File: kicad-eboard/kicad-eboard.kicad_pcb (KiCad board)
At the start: 2 copper layers, 93 parts, among them J1 Conn_02x03, J2 Conn_01x02, J3 Conn_01x10, M1 Hopper_Servo, SW1 LIMIT_1, SW2 LIMIT_2, SW3 SRX_Encoder, U1 TinkerBoard, U10 REF2033, U11 PDQ15-Q24-S12-D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

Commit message: More routing, moving components
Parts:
- C20, C21, R12, R15: moved to B.Cu
- moved TP5 90.6 mm to (72.6, 93.8)
- moved TP6 90.6 mm to (69.6, 93.8)
- moved H1 71.5 mm to (28.4, 36.9)
- moved H2 71.5 mm to (28.4, 94.9)
- moved H3 71.5 mm to (77.4, 36.9)
- moved H4 71.5 mm to (77.4, 94.9)
- moved R15 68.0 mm to (56.1, 81.2), turned to 180 degrees
- moved R12 66.4 mm to (59.8, 81.2), turned to 0 degrees
- moved TP13 55.3 mm to (69.5, 35.2)
- moved TP1 52.1 mm to (28.9, 23.9)
- moved TP12 42.2 mm to (92.4, 38.2), turned to 270 degrees
- moved TP14 37.8 mm to (71.9, 30.9)
- moved TP15 37.8 mm to (71.9, 27.6)
- moved TP9 34.3 mm to (65.1, 18.3), turned to 0 degrees
- moved TP11 33.6 mm to (92.4, 31.5), turned to 90 degrees
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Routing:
- net /M1+: track 15.0 -> 13.8 mm

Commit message: Finish routing?
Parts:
- moved C3 52.8 mm to (29.8, 103.7)
- moved M1 28.8 mm to (46.5, 102.2)
- moved TP15 21.6 mm to (79.7, 47.7), turned to 270 degrees
- moved RV1 17.7 mm to (57.6, 102.2)
- moved RV2 17.7 mm to (68.6, 102.2)
- moved RV3 17.7 mm to (79.6, 102.2)
- moved L1 15.3 mm to (47.5, 54.8)
- moved TP12 13.3 mm to (79.6, 41.8)
- moved C9 12.9 mm to (58.8, 19.6)
- moved TP11 12.5 mm to (80.0, 32.5)
- moved C12 11.7 mm to (48.9, 21.5)
- moved C16 11.0 mm to (42.8, 23.4)
- moved TP13 8.64 mm to (76.2, 29.8), turned to 270 degrees
- moved C14 6.86 mm to (44.9, 23.4), turned to 270 degrees
- moved SW3 5.41 mm to (30.6, 41.6), turned to 270 degrees
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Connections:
- U1 pad 16: Net-(U1-Pad16) -> /IMU/INT
- U1 pad 27: /IMU/INT -> Net-(U1-Pad27)
- U8 pad 4: Net-(RV1-Pad2) -> Net-(M1-Pad4)
- U8 pad 5: Net-(RV2-Pad2) -> Net-(RV1-Pad2)
- U8 pad 6: Net-(RV3-Pad2) -> Net-(RV2-Pad2)
- U8 pad 7: Net-(M1-Pad4) -> Net-(RV3-Pad2)
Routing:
- net +5V: track 9.19 -> 202.8 mm, vias 1 -> 2
- net GNDA: track 0.00 -> 163.3 mm
- net +12V: track 0.00 -> 140.7 mm
- net +3V3: track 67.0 -> 188.9 mm, vias 3 -> 4
- net GND: track 47.1 -> 133.5 mm, vias 2 -> 4
- net GNDPWR: track 0.00 -> 84.2 mm
- net /SDA: track 28.3 -> 97.5 mm
- net /SCL: track 38.8 -> 101.6 mm, vias 0 -> 1
- net Net-(TP1-Pad1): track 0.00 -> 60.6 mm, vias 0 -> 1
- net +BATT: track 0.00 -> 54.1 mm
- net Net-(C20-Pad1): track 0.00 -> 52.4 mm
- net /SCLK: track 11.7 -> 60.0 mm, vias 0 -> 1
- net /MISO: track 6.95 -> 52.9 mm, vias 0 -> 1
- net /SS: track 6.24 -> 51.2 mm, vias 0 -> 1
- net /MOSI: track 3.28 -> 46.9 mm, vias 0 -> 1
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- added copper zone on B.Cu, net GND
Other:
- board outline added: 67.2 x 90 mm
- copper layers 2 -> 4

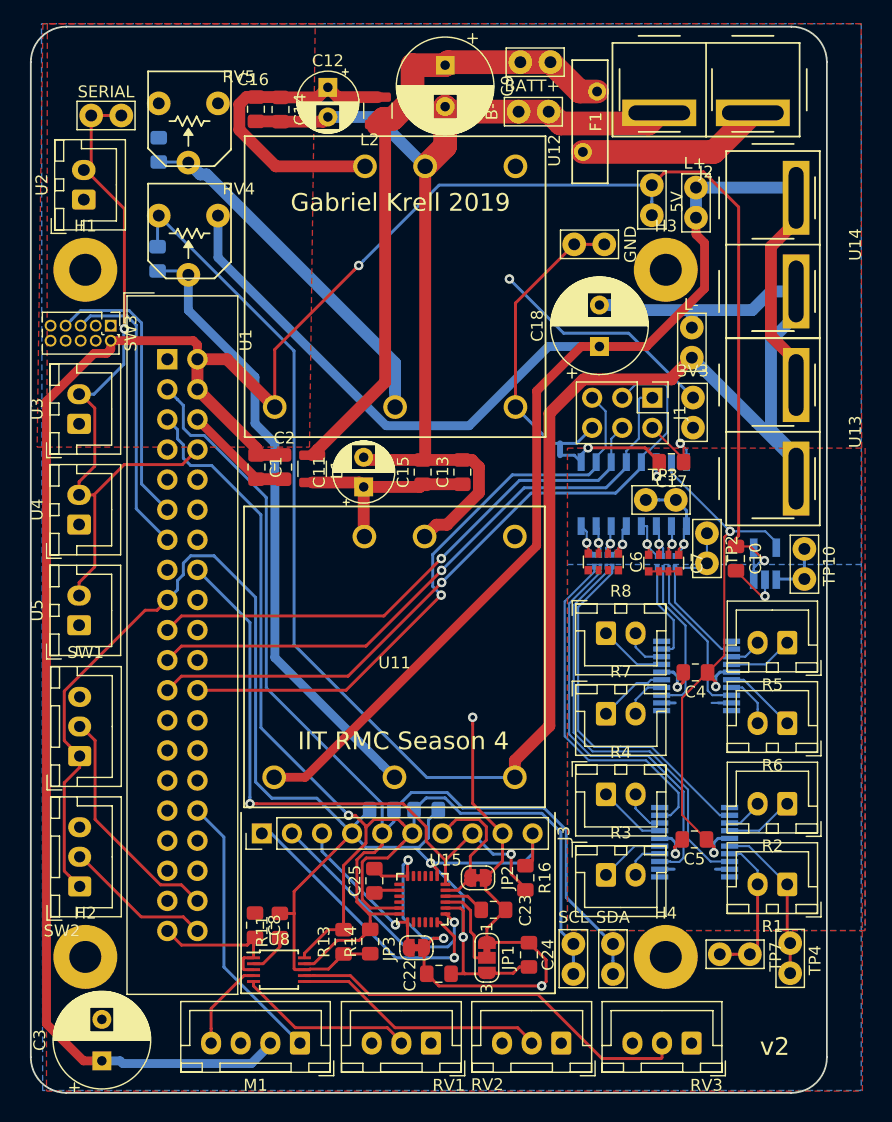
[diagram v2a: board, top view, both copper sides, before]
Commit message: Silkscreen cleanup
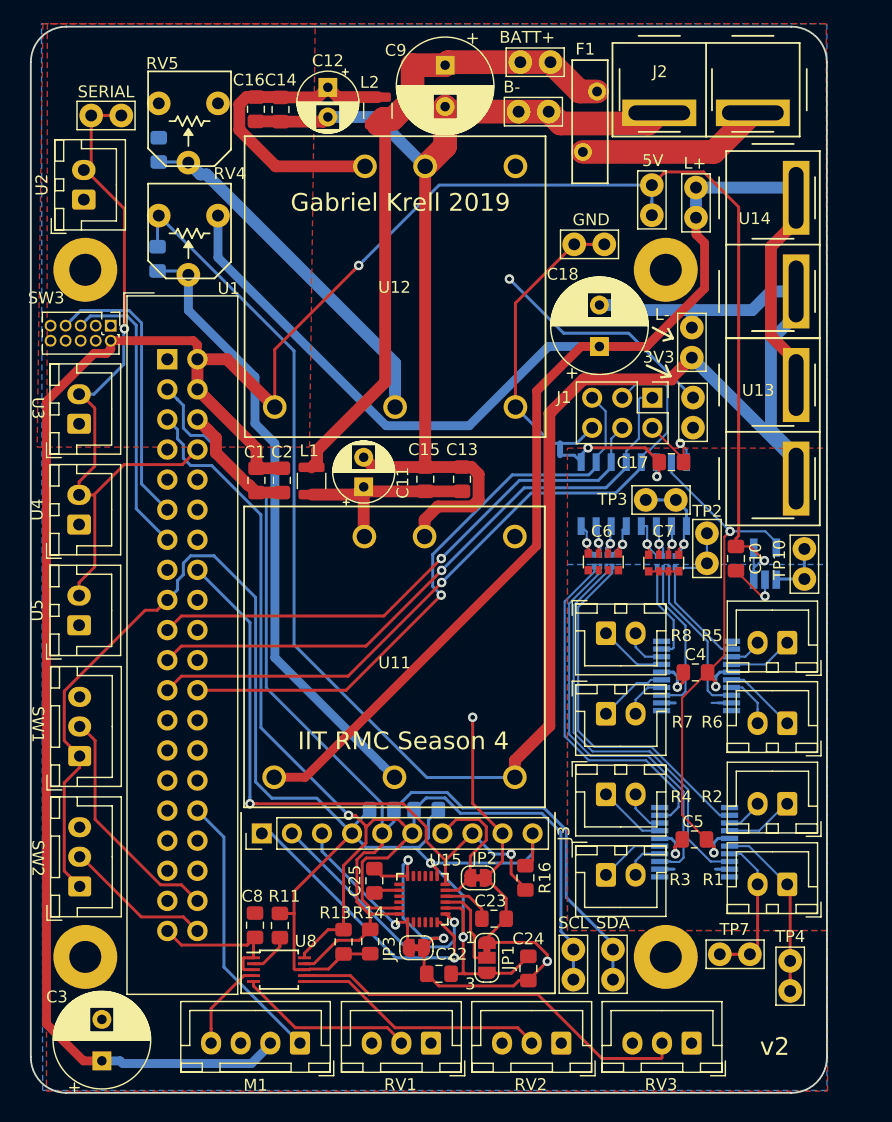
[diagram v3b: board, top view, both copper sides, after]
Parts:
- moved TP4 1.50 mm to (87.9, 97.8)
- moved C24 1.15 mm to (65.8, 95.9), turned to 270 degrees
- moved C2 1.13 mm to (45.0, 54.7)
- moved C1 1.12 mm to (42.9, 54.7)
- moved L1 1.03 mm to (47.5, 55.8)
- moved C23 0.75 mm to (62.9, 91.7)
- moved C15 0.64 mm to (57.1, 54.6)
- moved C13 0.60 mm to (60.2, 54.6)
- moved TP6 0.47 mm to (69.6, 94.3)
- moved TP5 0.47 mm to (72.9, 94.3)
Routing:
- net GNDPWR: track 84.2 -> 85.8 mm
- net /M1+: track 13.8 -> 15.3 mm
- net +BATT: track 54.1 -> 55.2 mm
- net +5V: track 202.8 -> 203.9 mm
- net Net-(C23-Pad1): track 3.50 -> 4.33 mm
- net GND: track 133.5 -> 134.1 mm

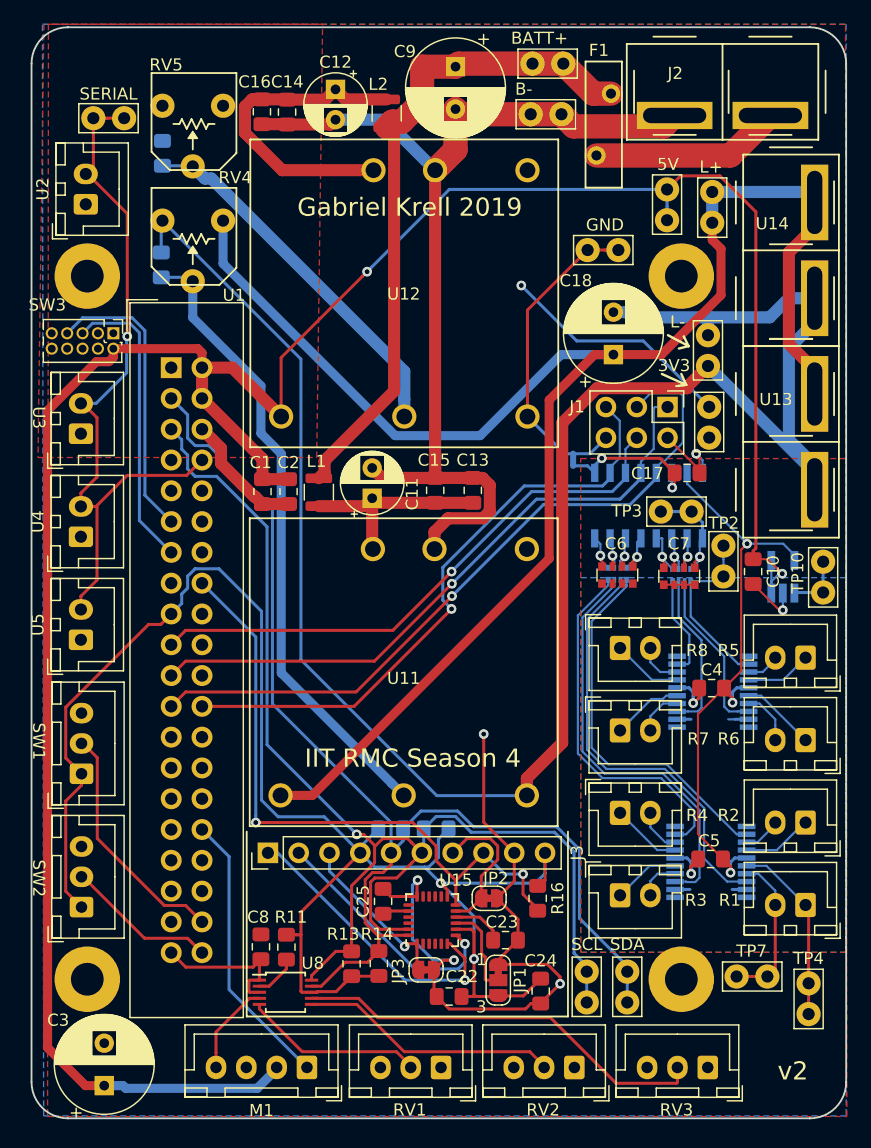
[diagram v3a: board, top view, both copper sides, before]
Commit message: Fix Powerpole 3D/connection issue; more silkscreen
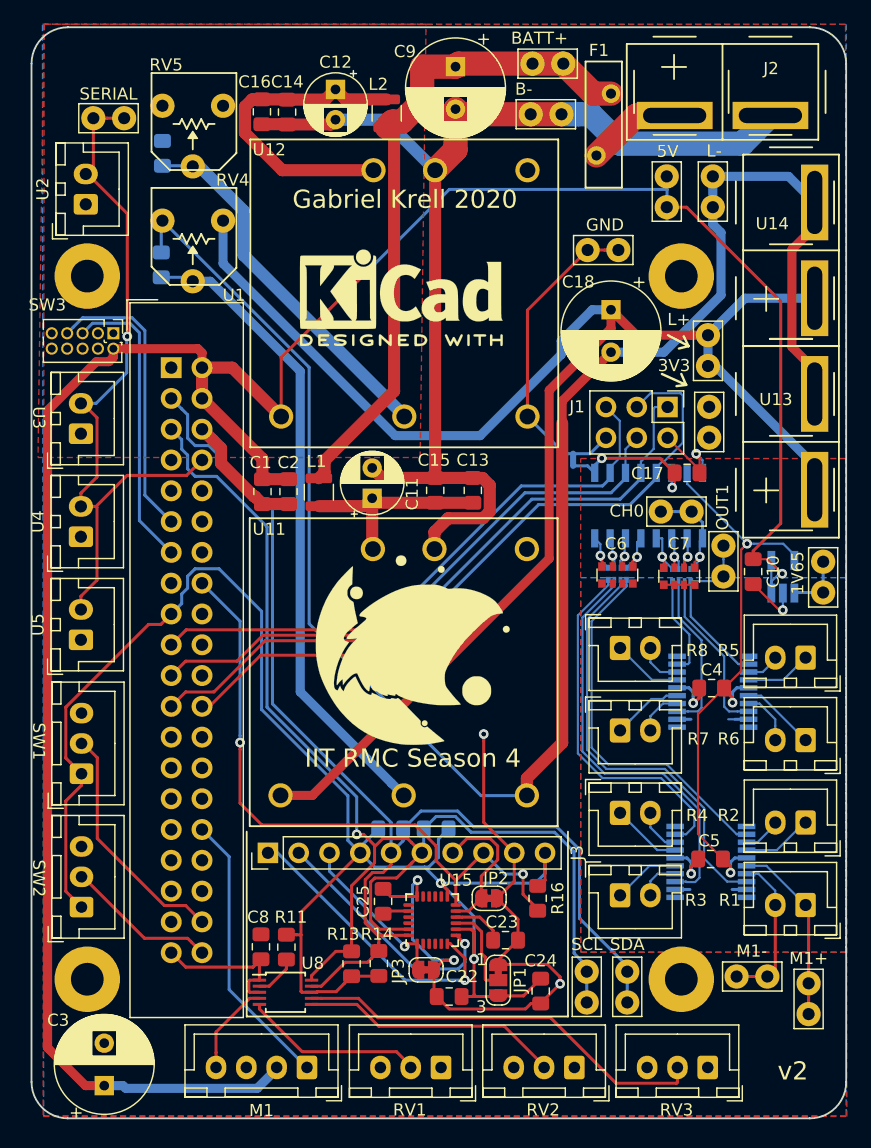
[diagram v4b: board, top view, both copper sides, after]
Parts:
- added G***: LOGO, 2019Spacehawks:SSH_logo, B.Cu at (54.4, 67.1)
- added G***: LOGO, 2019Spacehawks:SSH_logo, F.Cu at (55.4, 67.3)
- added G1: KiCad-Logo2_8mm_SilkScreen, Symbol:KiCad-Logo2_8mm_SilkScreen, B.Cu at (54.9, 38.7)
- added G1: KiCad-Logo2_8mm_SilkScreen, Symbol:KiCad-Logo2_8mm_SilkScreen, F.Cu at (54.3, 38.7)
- moved TP12 13.1 mm to (80.0, 28.7)
- moved TP11 11.8 mm to (79.6, 44.3)
- moved C18 3.71 mm to (71.6, 39.7), turned to 270 degrees
- moved TP13 1.08 mm to (76.2, 28.7)
- renumbered TP10 to 1V65, TP3 to CH0, TP4 to M1+, TP7 to M1-, TP2 to OUT1
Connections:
- J2 pad 1: Net-(F1-Pad1) -> GNDPWR
- J2 pad 2: GNDPWR -> Net-(F1-Pad1)
- U13 pad 1: +12V -> GNDA
- U13 pad 2: GNDA -> +12V
- U14 pad 1: +12V -> GNDA
- U14 pad 2: GNDA -> +12V
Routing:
- net +3V3: track 189.2 -> 167.4 mm, vias 4 -> 3
- net GNDA: track 163.3 -> 151.9 mm
- net GNDPWR: track 85.8 -> 94.9 mm
- net Net-(F1-Pad1): track 15.7 -> 7.82 mm
- net +12V: track 140.7 -> 137.0 mm
- net +5V: track 203.9 -> 200.9 mm
- net /SS: track 51.2 -> 50.2 mm
- net Net-(C20-Pad1): track 52.4 -> 53.2 mm
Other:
- board text added: "Gabriel Krell 2020"
- board text added: "extra I2C pull-ups"
- board text removed: "Gabriel Krell 2019"

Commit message: Fix test point labels (oops)
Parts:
- renumbered 1V65 to TP10, OUT1 to TP2, CH0 to TP3, M1+ to TP4, M1- to TP7

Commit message: Add logo symbols, standardize component values
Added a hacky almost-invisible schematic symbol for graphics, because
otherwise hitting "Update PCB from Schematic" will delete footprints
that aren't in the schematic. Also standardized component values - prefer
100n to 0.1u; prefer 100n to 100nF; prefer 100k to 100K.
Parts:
- C10, C17, C23, C24, C4, C5, C8: value 0.1uF -> 100n
- C22: value 10nF -> 10n
- C25: value 2.2nF -> 2.2n
- C9: value 1000uF -> 1000u
- G1: value KiCad-Logo2_8mm_SilkScreen -> Logo
- G2: renamed from G1; value KiCad-Logo2_8mm_SilkScreen -> Logo
- G3, G4: renamed from G***; value LOGO -> Logo
- R11, R12, R13, R14, R15, R16, RV1, RV2, RV3, RV4, RV5: value 10K -> 10k

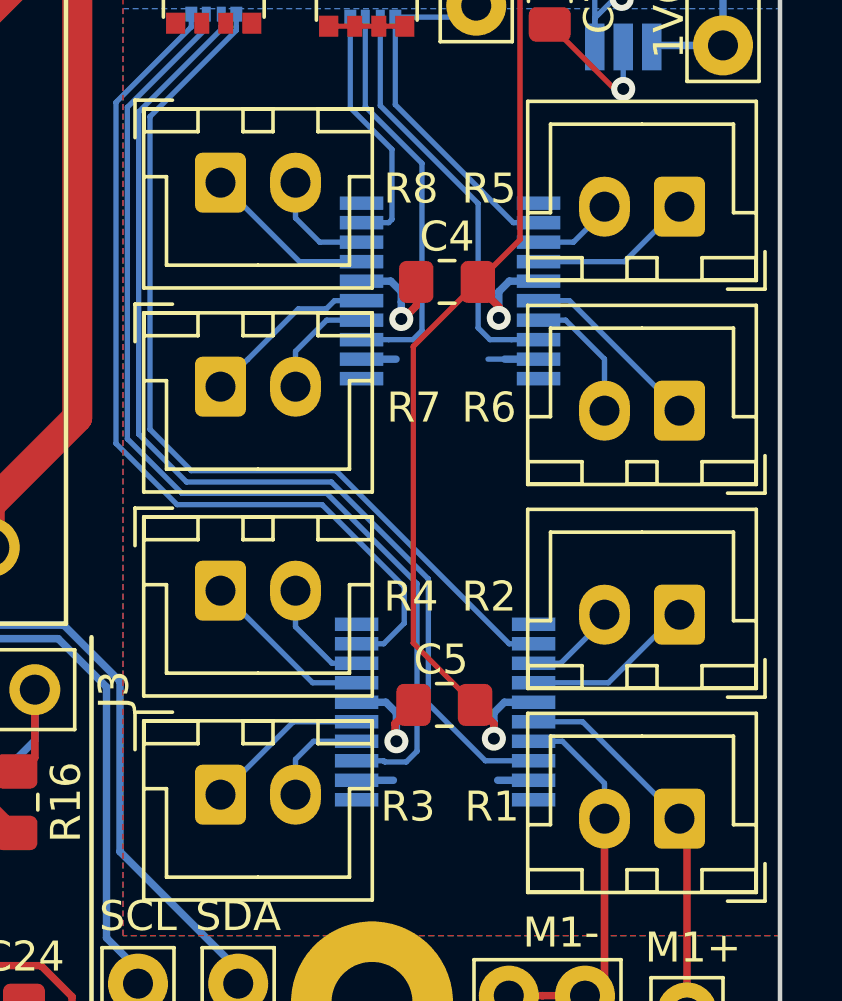
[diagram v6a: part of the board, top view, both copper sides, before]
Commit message: Length match current sense leads
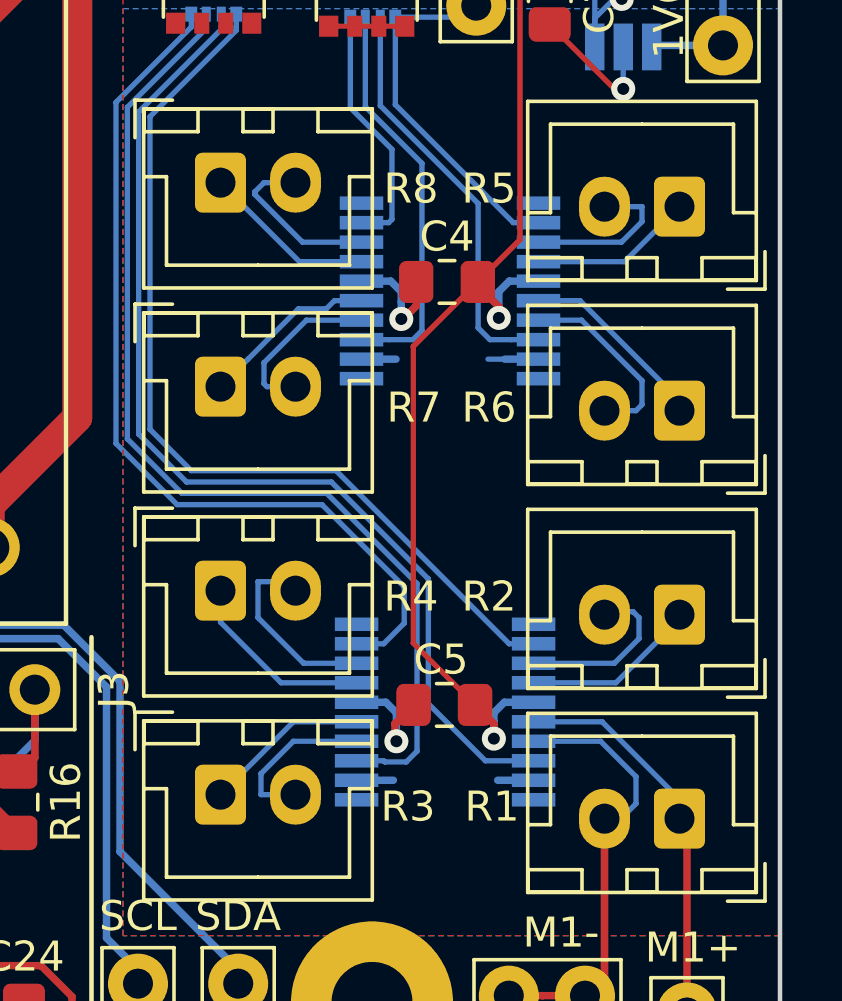
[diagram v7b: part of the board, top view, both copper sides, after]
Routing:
- net /M4-: track 3.74 -> 6.49 mm
- net /M5-: track 2.78 -> 5.48 mm
- net /M2-: track 3.23 -> 5.79 mm
- net /M8-: track 3.71 -> 5.79 mm
- net /M3-: track 3.46 -> 5.48 mm
- net /M6-: track 4.46 -> 6.42 mm
- net /M1-: track 12.8 -> 14.8 mm
- net /M7-: track 3.81 -> 5.63 mm
- net /M4+: track 5.81 -> 6.42 mm
